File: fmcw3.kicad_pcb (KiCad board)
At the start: 6 copper layers, 104 x 47.7 mm, 397 parts, among them CON1 SD_Card_DM3BT, CON2 BARREL_JACK, J1 USB_C_Receptacle_USB2.0, J2 Connector_02x08, P1 SMA, P2 SMA, P5 CONN_01X01, P7 CONN_01X01, P8 CONN_01X01, SW1 B3U-1000P, SW2 B3U-1000P, U1 ADF4158, U10 HMC431LP4, U11 SKY65404, U12 PAT1220-3dB, U13 TRF37A73, U14 TQP5525, U15 SMA, U16 SKY65404, U17 LMR51420, U18 LMR51420, U19 LMR51420, U2 SolderPad_1_Circle, U20 LP5907-3.0, U21 LP2985A-10DBVR, U22 LD3920, U23 LD3920, U24 LD3920, U25 BU33SD5WG, U26 5400BL15B0050001E, U27 5400BL15B0050001E, U28 5400BL15B0050001E, U29 ADL5802, U3 PAT1220-6dB, U30 XC7A35T-1FTG256C, U31 SolderPad_1_Circle, U32 93LC46B, U33 FT2232H, U34 SolderPad_1_Circle, U35 SolderPad_1_Circle, U36 SolderPad_1_Circle, U38 SolderPad_1_Circle, U39 LP5907-3.0, U4 SolderPad_1_Circle, U40 W25Q128JV, U41 SolderPad_1_Circle, U42 SolderPad_1_Circle, U43 SolderPad_1_Circle, U44 SolderPad_1_Circle, U45 LT6232, U46 SolderPad_1_Circle, U47 SolderPad_1_Circle, U48 SolderPad_1_Circle, U49 SolderPad_1_Circle, U5 SolderPad_1_Circle, U6 PL133-37, U7 TLV172DCK, U8 LTC2292, U9 TRF37A73, Y1 ABM10-167-12.000MHZ-T3, Y2 ECS-TXO-32CSMV

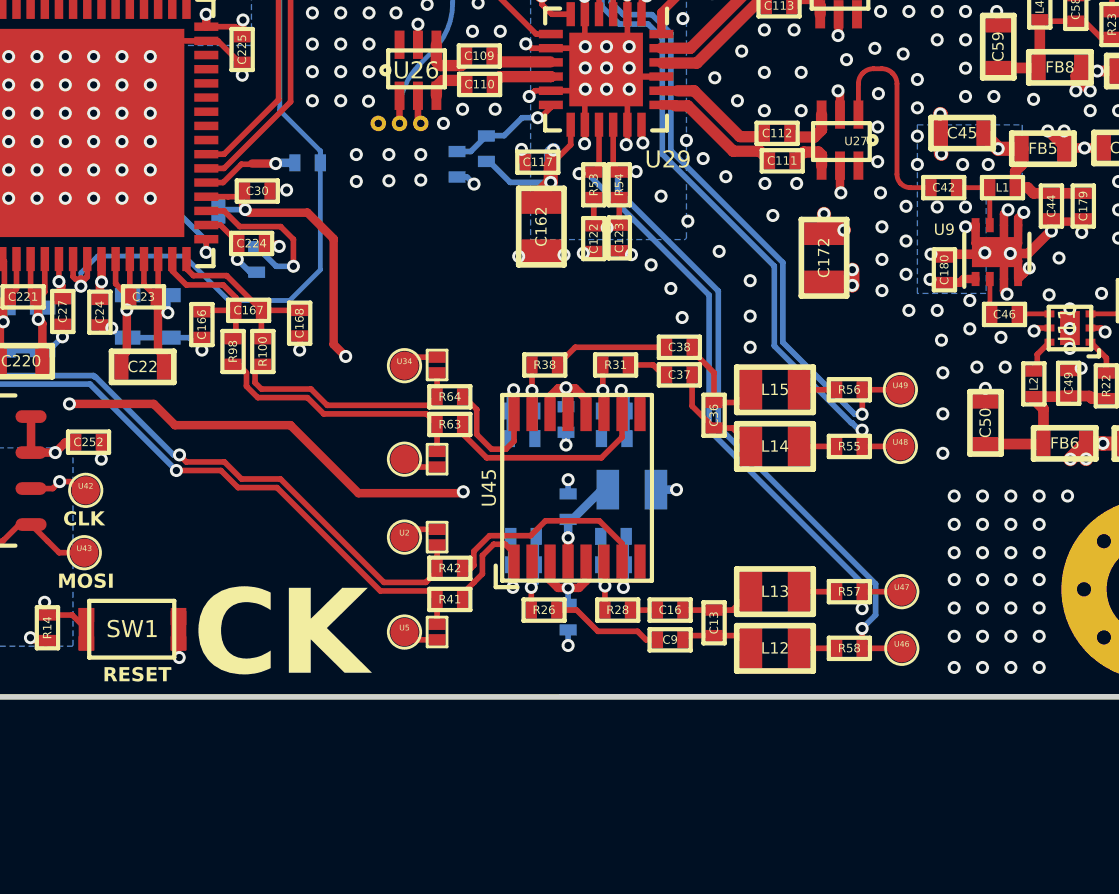
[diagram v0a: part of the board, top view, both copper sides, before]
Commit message: regulator cooper pours are continuous it is checked. gnd vias will be added
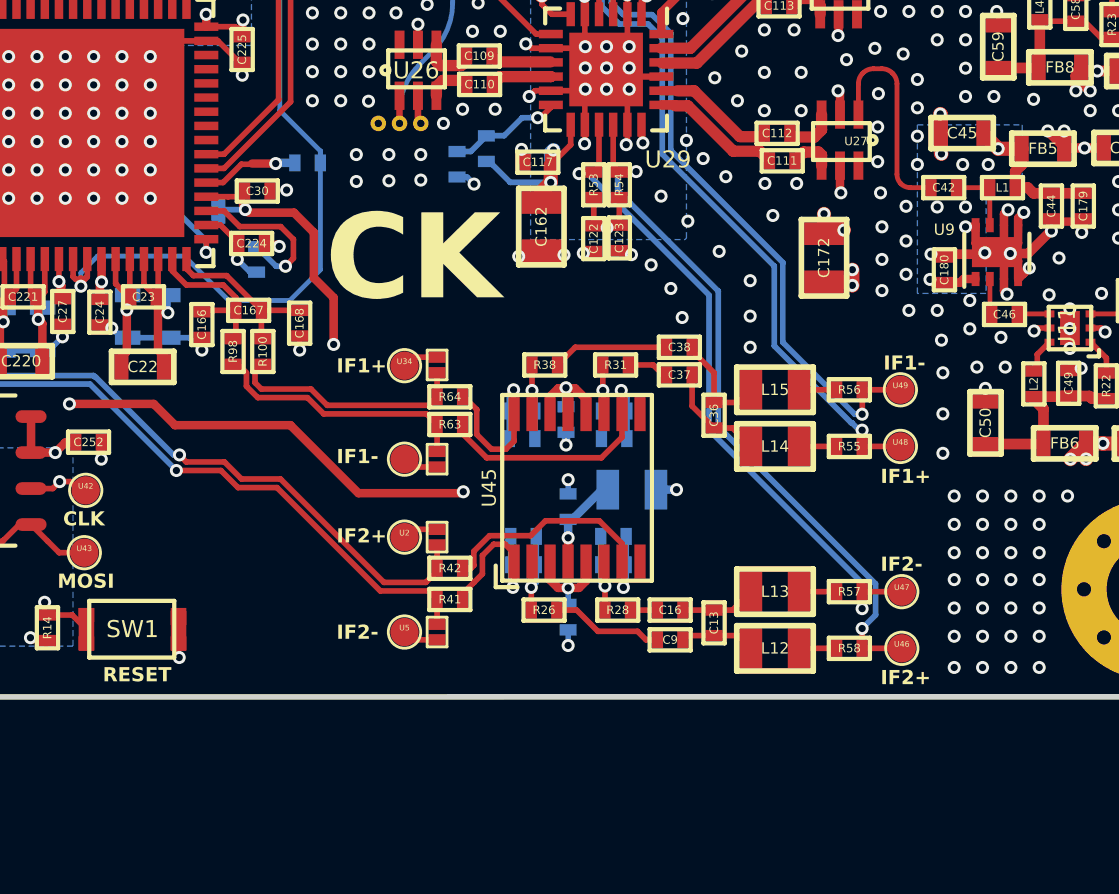
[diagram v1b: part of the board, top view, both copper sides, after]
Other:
- board text added: "IF1+"
- board text added: "IF1-"
- board text added: "IF2+"
- board text added: "IF2-"
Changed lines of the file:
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@@
 		)
 	)
+	(gr_text "IF1+"
+		(at 182.4 107 0)
+		(layer "F.SilkS")
+		(effects
+			(font
+				(size 0.5 0.5)
+				(thickness 0.125)
+				(bold yes)
+			)
+			(justify left bottom)
+		)
+	)
 	(gr_text "PIN10"
 		(at 136.05 107.8 0)
@@
 		)
 	)
+	(gr_text "IF2-"
+		(at 163.2 112.5 0)
+		(layer "F.SilkS")
+		(effects
+			(font
+				(size 0.5 0.5)
+				(thickness 0.125)
+				(bold yes)
+			)
+			(justify left bottom)
+		)
+	)
 	(gr_text "CLK"
 		(at 153.55 108.5 0)
@@
 	)
 	(gr_text "CK"
-		(at 161.225 112.25 0)
+		(at 165.9 99 0)
 		(layer "F.SilkS")
 		(effects
@@
 		)
 	)
+	(gr_text "IF1-"
+		(at 182.5 103 0)
+		(layer "F.SilkS")
+		(effects
+			(font
+				(size 0.5 0.5)
+				(thickness 0.125)
+				(bold yes)
+			)
+			(justify left bottom)
+		)
+	)
 	(gr_text "PIN12"
 		(at 141.2 107.8 0)
@@
 		)
 	)
+	(gr_text "IF2+"
+		(at 182.4 114.1 0)
+		(layer "F.SilkS")
+		(effects
+			(font
+				(size 0.5 0.5)
+				(thickness 0.125)
+				(bold yes)
+			)
+			(justify left bottom)
+		)
+	)
 	(gr_text "MOSI"
 		(at 153.35 110.7 0)
@@
 		)
 	)
+	(gr_text "IF2+"
+		(at 163.2 109.1 0)
+		(layer "F.SilkS")
+		(effects
+			(font
+				(size 0.5 0.5)
+				(thickness 0.125)
+				(bold yes)
+			)
+			(justify left bottom)
+		)
+	)
 	(gr_text "STATUS"
 		(at 119.35 113.35 0)
@@
 		)
 	)
+	(gr_text "IF2-"
+		(at 182.4 110.1 0)
+		(layer "F.SilkS")
+		(effects
+			(font
+				(size 0.5 0.5)
+				(thickness 0.125)
+				(bold yes)
+			)
+			(justify left bottom)
+		)
+	)
 	(gr_text "PIN4"
 		(at 128.45 114.1 0)
@@
 		)
 	)
+	(gr_text "IF1-"
+		(at 163.2 106.3 0)
+		(layer "F.SilkS")
+		(effects
+			(font
+				(size 0.5 0.5)
+				(thickness 0.125)
+				(bold yes)
+			)
+			(justify left bottom)
+		)
+	)
 	(gr_text "PIN11"
 		(at 138.65 107.8 0)
@@
 		)
 	)
+	(gr_text "IF1+"
+		(at 163.2 103.1 0)
+		(layer "F.SilkS")
+		(effects
+			(font
+				(size 0.5 0.5)
+				(thickness 0.125)
+				(bold yes)
+			)
+			(justify left bottom)
+		)
+	)
 	(gr_text "ADF_REF"
 		(at 144.597605 82.115217 0)
@@
 	)
 	(segment
-		(start 160.0224 103.525341)
-		(end 160.0224 103.0474)
+		(start 166.75 105.825)
+		(end 166.75 104.875)
 		(width 0.2)
 		(layer "F.Cu")
@@
 	)
 	(segment
-		(start 166.75 104.875)
-		(end 166.3776 104.5026)
+		(start 160.424658 103.9276)
+		(end 160.0224 103.525341)
 		(width 0.2)
 		(layer "F.Cu")
@@
 	)
 	(segment
-		(start 166.75 105.825)
-		(end 166.75 104.875)
+		(start 166.3776 104.5026)
+		(end 162.749658 104.5026)
 		(width 0.2)
 		(layer "F.Cu")
@@
 	)
 	(segment
-		(start 159.725 102.75)
-		(end 159.55 102.75)
+		(start 162.749658 104.5026)
+		(end 162.174658 103.9276)
 		(width 0.2)
 		(layer "F.Cu")
@@
 	)
 	(segment
-		(start 160.424658 103.9276)
-		(end 160.0224 103.525341)
+		(start 166.75 104.875)
+		(end 166.3776 104.5026)
 		(width 0.2)
 		(layer "F.Cu")
@@
 	)
 	(segment
-		(start 166.3776 104.5026)
-		(end 162.749658 104.5026)
+		(start 159.725 102.75)
+		(end 159.55 102.75)
 		(width 0.2)
 		(layer "F.Cu")
@@
 	)
 	(segment
-		(start 162.749658 104.5026)
-		(end 162.174658 103.9276)
+		(start 162.174658 103.9276)
+		(end 160.424658 103.9276)
 		(width 0.2)
 		(layer "F.Cu")
@@
 	)
 	(segment
-		(start 162.174658 103.9276)
-		(end 160.424658 103.9276)
+		(start 160.0224 103.525341)
+		(end 160.0224 103.0474)
 		(width 0.2)
 		(layer "F.Cu")
@@
 	)
 	(segment
-		(start 159.230755 97.337524)
-		(end 159.785061 97.89183)
+		(start 161.680219 99.011611)
+		(end 161.680219 98.34183)
 		(width 0.2)
 		(layer "F.Cu")
@@
 	)
 	(segment
-		(start 158.605755 97.337524)
-		(end 159.230755 97.337524)
+		(start 161.4 99.29183)
+		(end 161.680219 99.011611)
 		(width 0.2)
 		(layer "F.Cu")
@@
 	)
 	(segment
-		(start 159.785061 97.89183)
-		(end 161.230219 97.89183)
+		(start 159.230755 97.337524)
+		(end 158.605755 97.337524)
 		(width 0.2)
 		(layer "F.Cu")
@@
 	)
 	(segment
-		(start 161.230219 97.89183)
-		(end 161.680219 98.34183)
+		(start 159.785061 97.89183)
+		(end 159.230755 97.337524)
 		(width 0.2)
 		(layer "F.Cu")
@@
 	(segment
 		(start 161.680219 98.34183)
-		(end 161.680219 99.29183)
+		(end 161.230219 97.89183)
+		(width 0.2)
+		(layer "F.Cu")
+		(net 138)
+	)
+	(segment
+		(start 161.230219 97.89183)
+		(end 159.785061 97.89183)
 		(width 0.2)
 		(layer "F.Cu")
@@
 	)
 	(via
-		(at 161.680219 99.29183)
+		(at 161.4 99.29183)
 		(size 0.46)
 		(drill 0.254)
@@
 	)
 	(segment
-		(start 161.680219 99.29183)
+		(start 161.4 99.29183)
 		(end 161.070219 99.29183)
 		(width 0.2)
@@
 	)
 	(segment
-		(start 163.525 102.475)
-		(end 163.1 102.05)
-		(width 0.3)
-		(layer "F.Cu")
-		(net 389)
-	)
-	(segment
 		(start 170.7368 110.3618)
 		(end 171.017302 110.642302)
@@
 	)
 	(segment
+		(start 161.7 97.4)
+		(end 160.088389 97.4)
+		(width 0.3)
+		(layer "F.Cu")
+		(net 389)
+	)
+	(segment
+		(start 162.4 99.7)
+		(end 162.4 98.1)
+		(width 0.3)
+		(layer "F.Cu")
+		(net 389)
+	)
+	(segment
+		(start 163.1 102.05)
+		(end 163.1 100.4)
+		(width 0.3)
+		(layer "F.Cu")
+		(net 389)
+	)
+	(segment
 		(start 172.0068 110.3932)
 		(end 171.757698 110.642302)
@@
 	)
 	(segment
-		(start 163.1 102.05)
-		(end 163.1 98.325)
-		(width 0.3)
-		(layer "F.Cu")
-		(net 389)
-	)
-	(segment
 		(start 159.855755 96.637524)
 		(end 159.855755 97.167366)
@@
 	)
 	(segment
-		(start 162.175 97.4)
-		(end 160.088389 97.4)
-		(width 0.3)
-		(layer "F.Cu")
-		(net 389)
-	)
-	(segment
 		(start 158.605755 96.837524)
 		(end 159.380219 96.837524)
@@
 	)
 	(segment
-		(start 163.1 98.325)
-		(end 162.175 97.4)
+		(start 162.4 98.1)
+		(end 161.7 97.4)
 		(width 0.3)
 		(layer "F.Cu")
@@
 		(net 389)
 	)
+	(segment
+		(start 163.1 100.4)
+		(end 162.4 99.7)
+		(width 0.3)
+		(layer "F.Cu")
+		(net 389)
+	)
 	(via
 		(at 159.980219 97.29183)
@@
 	)
 	(via
-		(at 163.525 102.475)
+		(at 163.1 102.05)
 		(size 0.46)
 		(drill 0.254)
@@
 	)
 	(segment
-		(start 170.232698 109.5)
-		(end 171.375 110.642302)
+		(start 163.1 102.05)
+		(end 164 102.95)
 		(width 0.3)
 		(layer "In3.Cu")
@@
 	)
 	(segment
-		(start 164 106.625)
-		(end 166.875 109.5)
+		(start 164 102.95)
+		(end 164 106.625)
 		(width 0.3)
 		(layer "In3.Cu")
@@
 	)
 	(segment
-		(start 164 102.95)
-		(end 164 106.625)
+		(start 166.875 109.5)
+		(end 170.232698 109.5)
 		(width 0.3)
 		(layer "In3.Cu")
@@
 	)
 	(segment
-		(start 163.525 102.475)
-		(end 164 102.95)
+		(start 164 106.625)
+		(end 166.875 109.5)
 		(width 0.3)
 		(layer "In3.Cu")
@@
 	)
 	(segment
-		(start 166.875 109.5)
-		(end 170.232698 109.5)
+		(start 170.232698 109.5)
+		(end 171.375 110.642302)
 		(width 0.3)
 		(layer "In3.Cu")
